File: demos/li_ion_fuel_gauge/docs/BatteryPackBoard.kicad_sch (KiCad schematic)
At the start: 10 parts, among them J1 Header1xNFemale

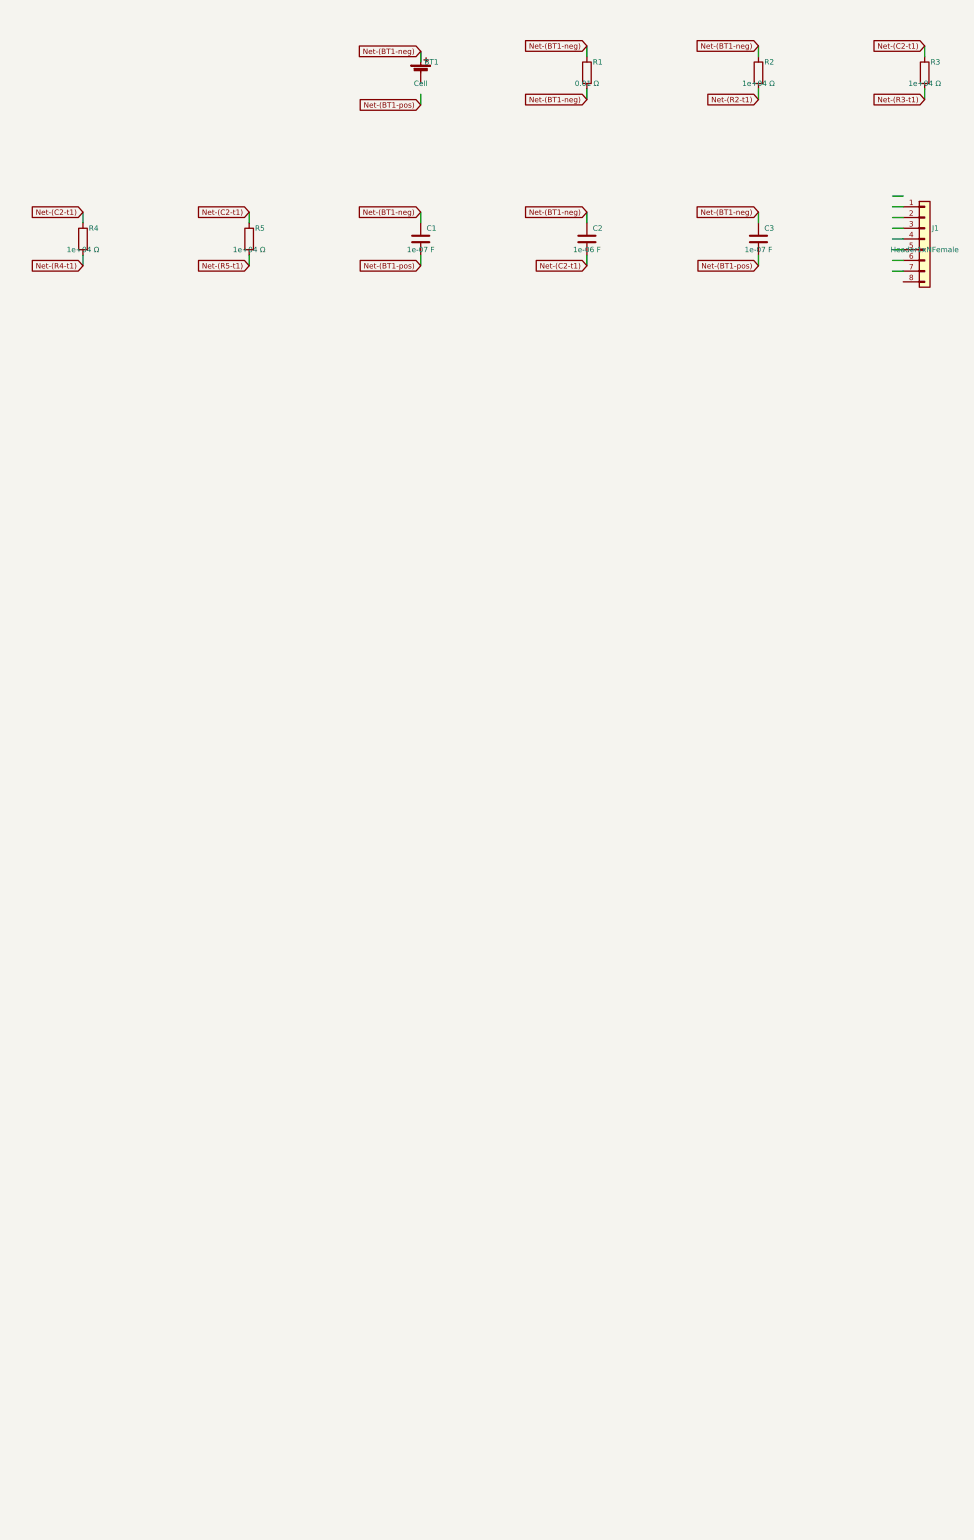
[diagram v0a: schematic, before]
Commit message: export: kicad_sch — Phase 2.5b: layered placement, wire routing, KiCad 10 compatibility (#23)
* export: kicad_sch — Phase 2.5b: layered placement + routing + KiCad 9 fix

Placement (placement.py, complete rewrite):
- Replaces naive grid with Layered Signal Flow algorithm (spec §5 stages 1–8)
- Stage 1: band classification — power chips/rails at top, LEDs at bottom,
  everything else in the signal band
- Stage 2: signal-flow DAG via BFS from Rail/Connector sources; layer = BFS
  distance from nearest source
- Stage 3–4: place within (band, layer) cells at 1500-mil (38.1 mm) same-band
  spacing, 1000-mil inter-band gutter, 25.4 mm page margin
- Stage 6: cluster breakup — up to 10 iterations shifting same-band parts
  that land closer than 0.9× SAME_BAND_SPACING_MM
- Stage 8: page sized to fit (A4 → A3 → A2 → A1)
- grid_place() and sheet_size_mm() kept as shims for backward-compat

Routing (routing.py, new file):
- route_net(): connects stub ends with Manhattan L-shapes (horizontal first)
- find_junctions(): returns points where ≥3 wire endpoints coincide
- renderer uses routed wires between signal-net stub ends

Hierarchical (hierarchical.py, new file):
- collect_boards(), is_multi_board(), sub_sheet_filename() — interface stub
  for multi-Board sub-sheet emission (full implementation deferred)

KiCad 9 sub-symbol name fix (library_loader.py):
- KiCad 9 schematics expect sub-symbols nested inside their parent in
  lib_symbols to use the bare name (R_0_1, LED_0_1, 4069_1_0) — NOT the
  lib-qualified name (Device:R_0_1, Device:LED_0_1, 4xxx:4069_1_0)
- Fixed _qualify_names() to add the lib: prefix only to the exact parent
  symbol name using a lookahead (?=") that prevents sub-unit names from
  being qualified

Tests (+25 tests):
- test_placement.py: band classification, all-on-grid, determinism,
  minimum spacing, power < signal < indicator Y ordering, page sizing
- test_routing.py: H/V segments, L-shapes, orthogonality, grid snap,
  junction detection

Golden files re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
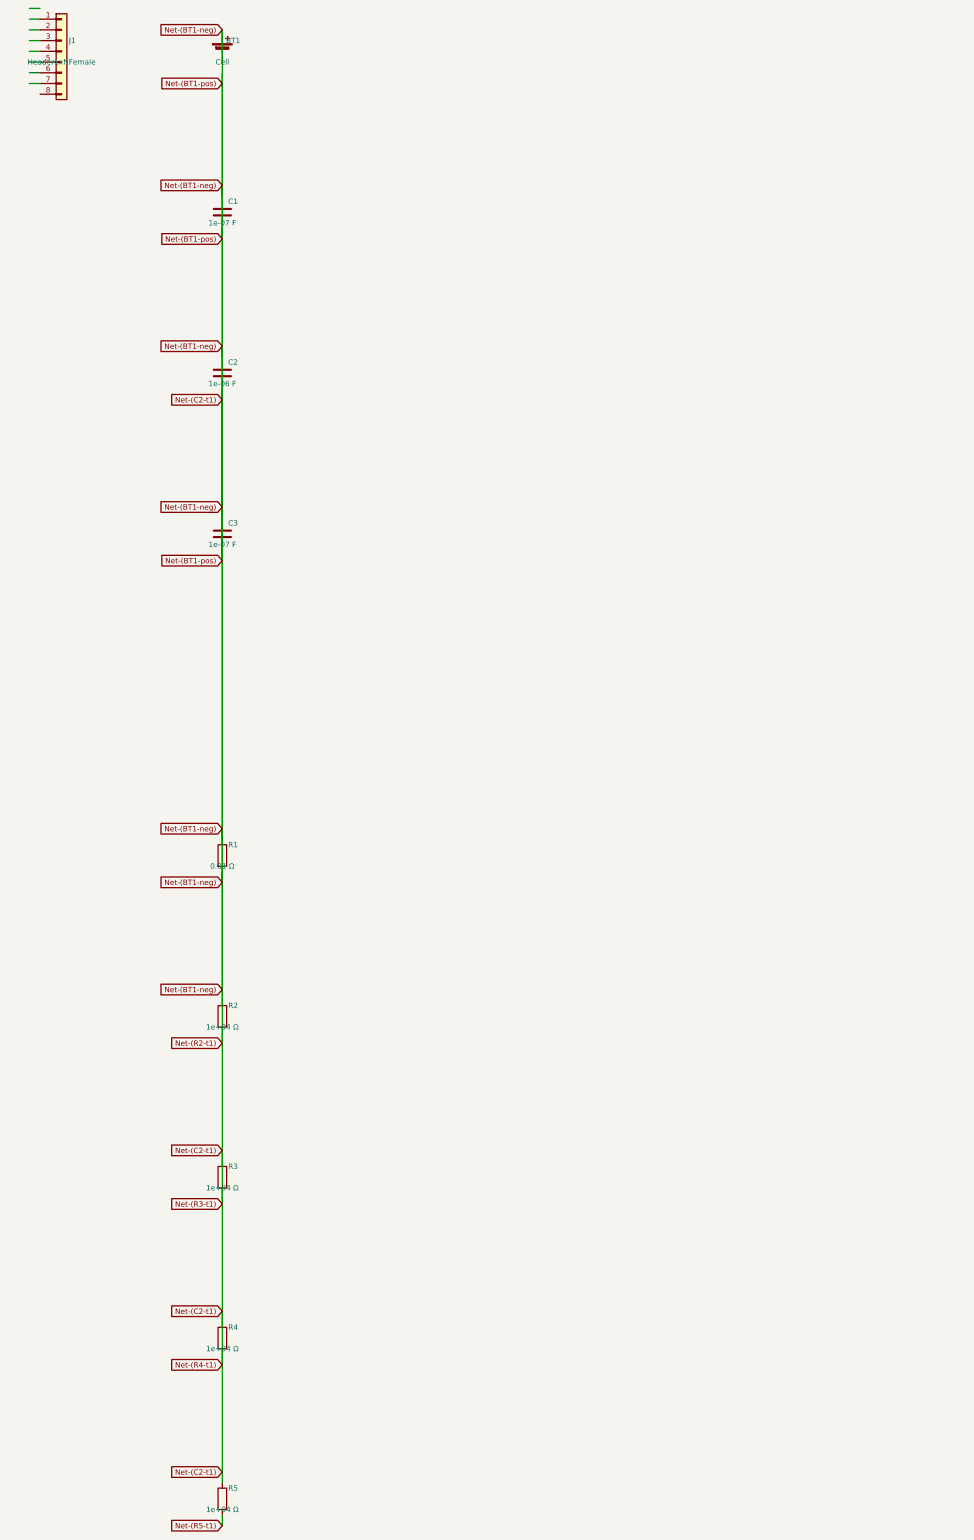
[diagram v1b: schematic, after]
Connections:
- net Net-(BT1-pos) is gone; now on net Net-(BT1-neg): C1.2, C3.2
- net Net-(C2-t1) is gone; now on net Net-(BT1-neg): C2.2, R3.1, R4.1, R5.1
- net Net-(R2-t1) is gone; now on net Net-(BT1-neg): R2.2
- net Net-(R3-t1) is gone; now on net Net-(BT1-neg): R3.2
- net Net-(R4-t1) is gone; now on net Net-(BT1-neg): R4.2
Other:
- moved on the sheet: BT1, C1, C2, C3, J1, R1, R2, R3, R4, R5

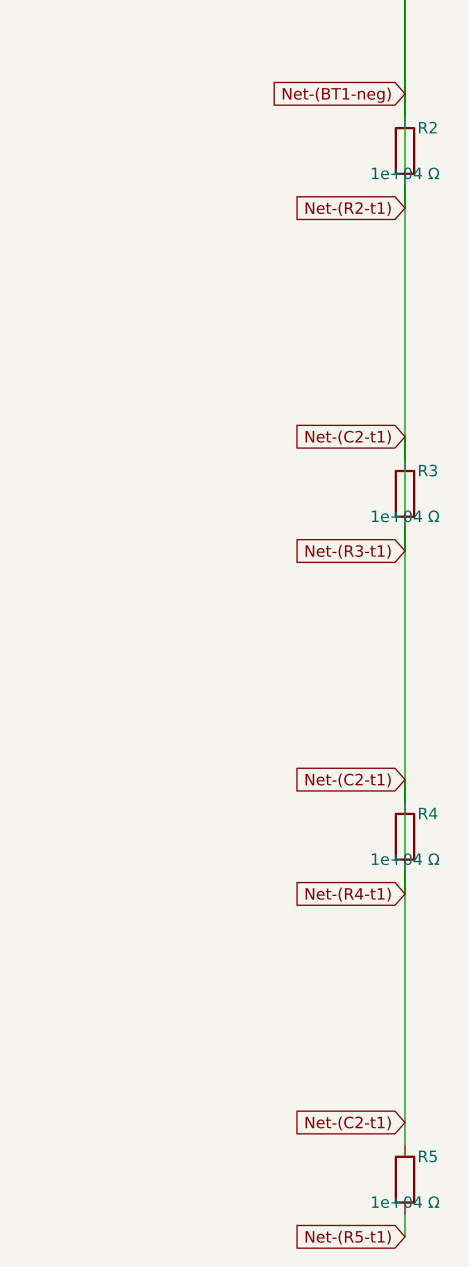
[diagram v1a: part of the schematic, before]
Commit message: units: Ohms.__str__ uses engineering notation (kΩ, MΩ, GΩ)
The previous `Ohms.__str__` formatted with bare `:.3g`, producing
unreadable scientific output for clean kilo / mega multiples:

  str(Ohms(10_000))     == "1e+04 Ω"      → now "10 kΩ"
  str(Ohms(100_000))    == "1e+05 Ω"      → now "100 kΩ"
  str(Ohms(1_000_000))  == "1e+06 Ω"      → now "1 MΩ"

The breadboard SVG visualiser surfaced the problem: a resistor body
labelled "100000Ω" makes a reader count zeros, while a label of
"100 kΩ" reads at a glance — exactly the convention every schematic
and parts catalogue uses. Centralising the engineering notation in
`Ohms.__str__` means every downstream consumer (assembly guide,
breadboard SVG, kicad netlist, BOM, reports) inherits the readable
form without each format adapter rolling its own formatter.

  - `Ohms.__str__` returns "47 Ω", "4.7 kΩ", "10 kΩ", "100 kΩ",
    "1 MΩ", "10 MΩ", "1 GΩ" per the kilo / mega / giga thresholds.
  - `Resistor.__str__` delegates to `str(self._ohms)` so it
    inherits the new notation (was producing the noisy "47.0 Ω"
    via raw float).
  - The breadboard visualiser's resistor body label uses
    `str(part.ohms)` directly (previously had a private
    `_format_ohms_compact` helper; removed).
  - `tests/components/test_resistor.py::test_str` updated for
    "47 Ω" (was "47.0 Ω"); new `test_str_renders_in_engineering_notation`
    pins kΩ / MΩ output across the kilo and mega thresholds.
  - All demo docs / goldens refreshed where the Ohms.__str__
    change affected the rendered output (breadboard SVGs, kicad
    sch value fields, BOM rows).
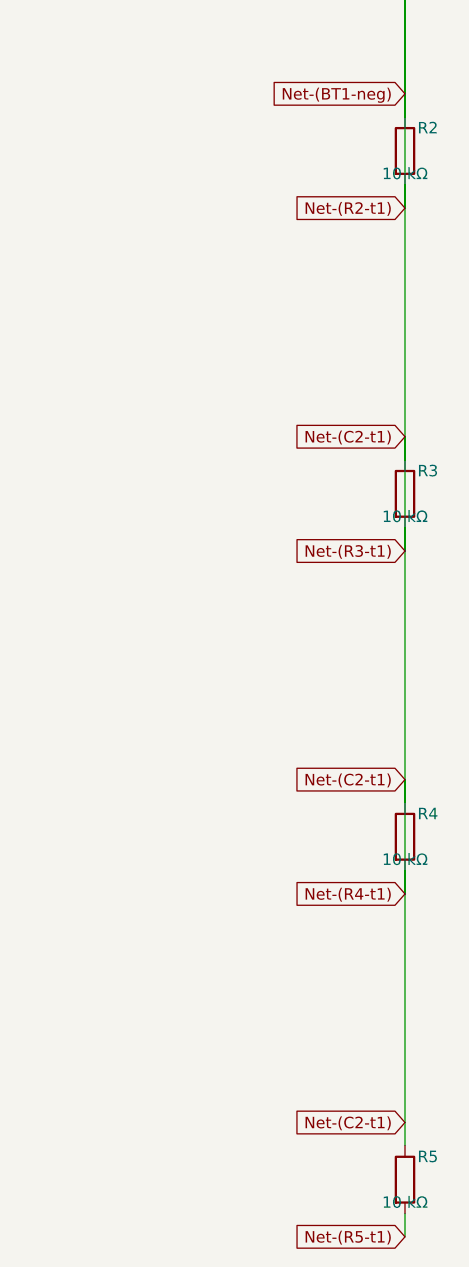
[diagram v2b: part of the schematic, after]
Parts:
- R2, R3, R4, R5: value 1e+04 Ω -> 10 kΩ
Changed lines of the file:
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@@
       (effects (font (size 1.27 1.27)))
     )
-    (property "Value" "1e+04 Ω"
+    (property "Value" "10 kΩ"
       (at 63.5 256.54 0)
       (effects (font (size 1.27 1.27)))
@@
       (effects (font (size 1.27 1.27)))
     )
-    (property "Value" "1e+04 Ω"
+    (property "Value" "10 kΩ"
       (at 63.5 294.64 0)
       (effects (font (size 1.27 1.27)))
@@
       (effects (font (size 1.27 1.27)))
     )
-    (property "Value" "1e+04 Ω"
+    (property "Value" "10 kΩ"
       (at 63.5 332.74 0)
       (effects (font (size 1.27 1.27)))
@@
       (effects (font (size 1.27 1.27)))
     )
-    (property "Value" "1e+04 Ω"
+    (property "Value" "10 kΩ"
       (at 63.5 370.84 0)
       (effects (font (size 1.27 1.27)))

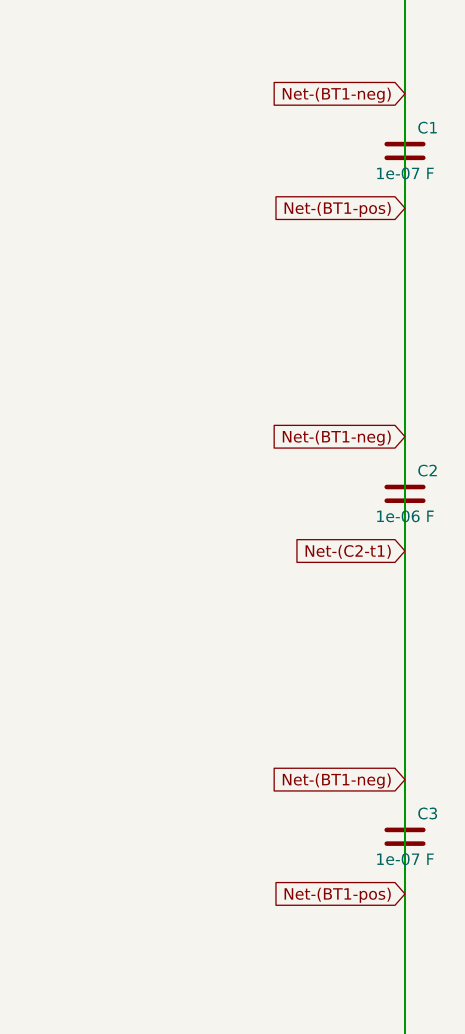
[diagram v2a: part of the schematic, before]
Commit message: units: Farads + Henries __str__ also use engineering notation
Same treatment as `Ohms.__str__` (previous commit) for the other two
passive engineering quantities. Demos contain caps and inductors
with values that the bare `:.3g` formatter would emit in scientific
form (`1e-07 F` for a 100 nF decoupling cap); centralising the
engineering notation on the unit class means every consumer
(reports, BOM, breadboard SVG, etc.) inherits the readable form.

  - `Farads.__str__` returns `100 pF`, `22 nF`, `100 nF`, `1 µF`,
    `4.7 µF`, `470 µF`, `1 mF`, `1 F` across the standard
    capacitance bands.
  - `Henries.__str__` returns `100 nH`, `10 µH`, `22 mH`, `1 H`
    across the standard inductance bands.
  - `Capacitor.__str__` and `Inductor.__str__` delegate to the
    unit class's str (were rolling raw-float formatters).
  - `framework.export.reports_common.part_description` now uses
    `str(part.ohms / farads / henries)` directly instead of the
    parallel `_format_ohms` / `_format_farads` / `_format_henries`
    helpers (removed — they duplicated the new logic on raw
    floats).
  - Breadboard SVG renderer now also labels capacitor and inductor
    bodies with their engineering-notation value (was only
    resistors).
  - `tests/framework/test_units.py`: parametrised regression tests
    for both unit classes across every band.
  - All affected demo docs / goldens refreshed.
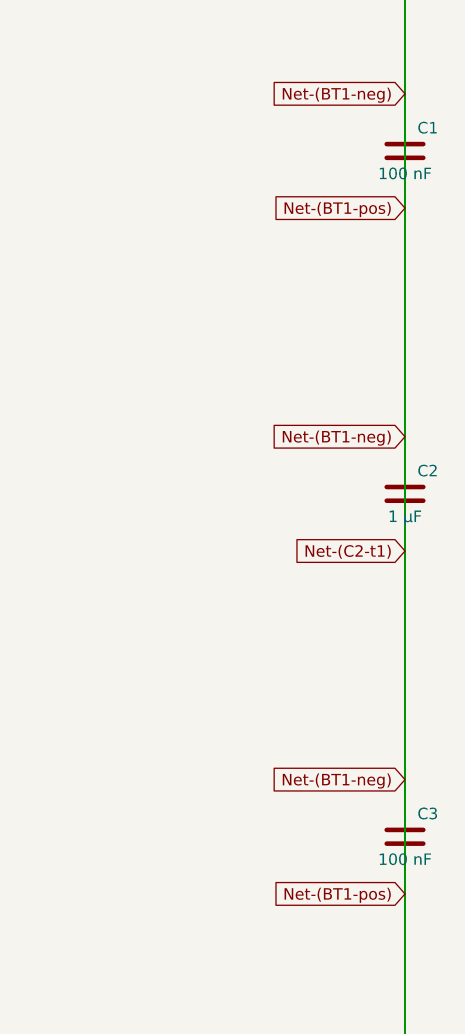
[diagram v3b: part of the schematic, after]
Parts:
- C1, C3: value 1e-07 F -> 100 nF
- C2: value 1e-06 F -> 1 µF
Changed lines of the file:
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@@
       (effects (font (size 1.27 1.27)))
     )
-    (property "Value" "1e-07 F"
+    (property "Value" "100 nF"
       (at 63.5 66.04 0)
       (effects (font (size 1.27 1.27)))
@@
       (effects (font (size 1.27 1.27)))
     )
-    (property "Value" "1e-06 F"
+    (property "Value" "1 µF"
       (at 63.5 104.14 0)
       (effects (font (size 1.27 1.27)))
@@
       (effects (font (size 1.27 1.27)))
     )
-    (property "Value" "1e-07 F"
+    (property "Value" "100 nF"
       (at 63.5 142.24 0)
       (effects (font (size 1.27 1.27)))
